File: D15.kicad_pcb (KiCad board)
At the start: 4 copper layers, 76 x 11 mm, 73 parts, among them IC1 DRV8847RTER, IC2 NCP730BM, J2 Conn_01x01, J3 Conn_01x01, J4 Conn_01x01, J5 UDPI, Q1 BC857BDW1, Q2 BC847BDW1, Q3 BC847BDW1, U1 AVR-64DA32, U3 BNO055, U4 TPS22810DRVR, m1 MountingHole_Pad

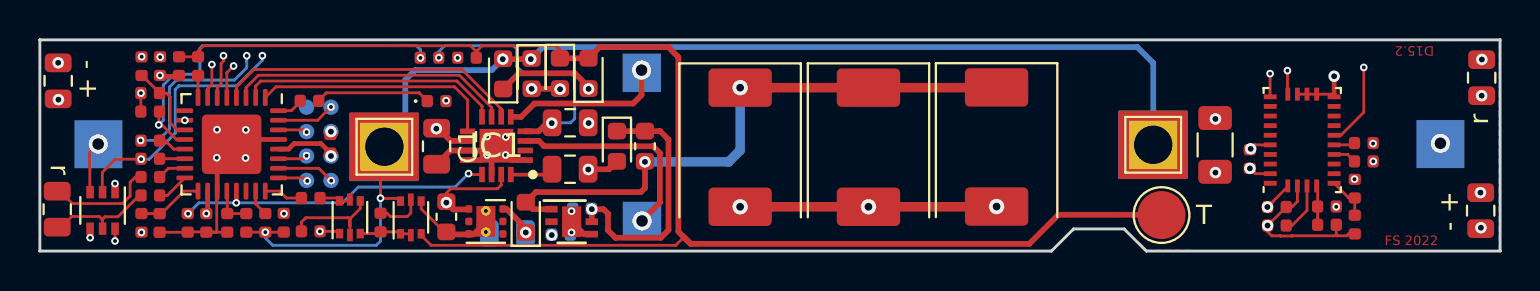
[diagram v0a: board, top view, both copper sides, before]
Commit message: Changed H-Bridge, added hardware PWM
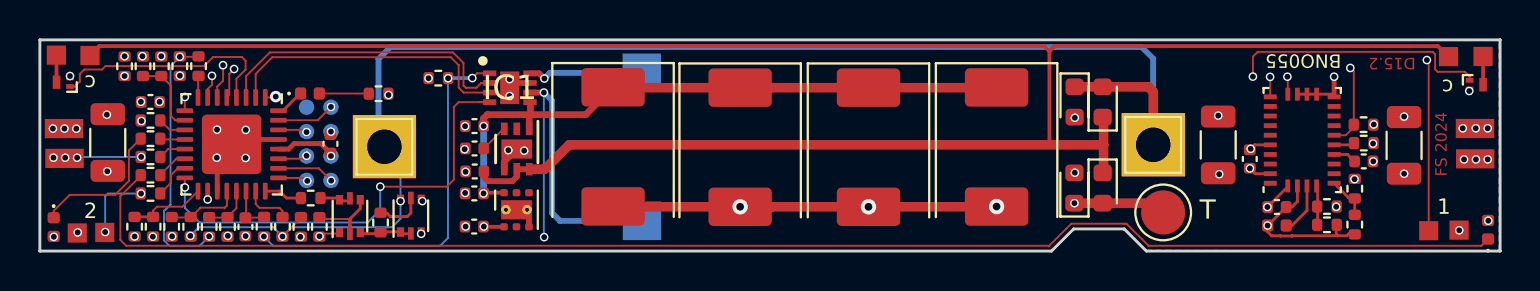
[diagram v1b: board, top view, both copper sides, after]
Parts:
- removed C16, C19, C20: Dummy, Capacitor_SMD:C_0805_2012Metric
- removed D9: CDBURT0530, Diode_SMD:D_0603_1608Metric
- removed H1, H3: MountingHole, TestPoint:TestPoint_THTPad_2.5x2.5mm_Drill1.2mm
- removed L1: 1uH, Inductor_SMD:L_0603_1608Metric
- added C3: 330u/25V, Capacitor_Tantalum_SMD:CP_EIA-7361-38_AVX-V, F.Cu at (80.1, -43.2)
- added C4: 220u/6V, Capacitor_SMD:C_1206_3216Metric, F.Cu at (111.6, -43.3)
- added D5: white, LED_SMD:LED_0402_1005Metric, F.Cu at (125.6, -38.9)
- added J1: Conn_01x01, RTB:DummyNet-Connector, F.Cu at (53.6, -38.7)
- added J10: Conn_01x01, RTB:DummyNet-Connector, F.Cu at (51.5, -44.1)
- added J11: Conn_01x01, RTB:DummyNet-Connector, F.Cu at (124.9, -44.1)
- added J12: Conn_01x01, RTB:DummyNet-Connector, F.Cu at (125.0, -42.5)
- added J13: Conn_01x01, RTB:DummyNet-Connector, F.Cu at (51.1, -48.0)
- added J14: Conn_01x01, RTB:DummyNet-Connector, F.Cu at (125.4, -47.9)
- added J15: Conn_01x01, RTB:DummyNet-Connector, F.Cu at (52.9, -47.9)
- added J16: Conn_01x01, RTB:DummyNet-Connector, F.Cu at (123.6, -47.9)
- added J6: Conn_01x01, RTB:DummyNet-Connector, F.Cu at (52.2, -38.7)
- added J7: Conn_01x01, RTB:DummyNet-Connector, F.Cu at (124.1, -38.8)
- added J8: Conn_01x01, RTB:DummyNet-Connector, F.Cu at (122.5, -38.8)
- added J9: Conn_01x01, RTB:DummyNet-Connector, F.Cu at (51.5, -42.6)
- added Q4: PMZB200UNEYL, Package_DFN_QFN:Diodes_DFN1006-3, F.Cu at (125.0, -46.4)
- added R27: 3.3k, Resistor_SMD:R_0402_1005Metric, F.Cu at (54.6, -47.4)
- C1: value 4.7u/25V -> 100n/50V; footprint Capacitor_SMD:C_0805_2012Metric -> Capacitor_SMD:C_0402_1005Metric
- C11: value 100u/16V -> 100n/50V; footprint Capacitor_SMD:C_0805_2012Metric -> Capacitor_SMD:C_0402_1005Metric; moved to F.Cu
- C12: value 47uF -> 4.7u/6V; footprint Capacitor_SMD:C_0603_1608Metric -> Capacitor_SMD:C_0402_1005Metric
- C14: value 220uF -> 220u/6V
- C15: value Dummy -> 220u/6V; footprint Capacitor_SMD:C_0805_2012Metric -> Capacitor_SMD:C_1206_3216Metric
- C17, C18, C7: value 100u/25V -> 330u/25V
- C2: value 2.2nF -> 100n; moved to F.Cu
- C5: value 100nF -> 100n/50V; moved to F.Cu
- D1: value CDBURT0530 -> white; footprint Diode_SMD:D_0603_1608Metric -> LED_SMD:LED_0402_1005Metric
- IC1: value DRV8847RTER -> DRV8231ADSGR; footprint _Samac:QFN50P300X300X80-17N-D -> RTB:SON50P200X200X80-9N
- J5: value UDPI -> UDPI & Debug IF
- Q3: value BC847BDW1 -> PMZB200UNEYL; footprint Package_TO_SOT_SMD:SOT-363_SC-70-6 -> Package_DFN_QFN:Diodes_DFN1006-3
- R10, R12: value 68k -> 47k
- R16: value 200 -> 3.3k; footprint Resistor_SMD:R_0805_2012Metric -> Resistor_SMD:R_0402_1005Metric
- R17: value 10k -> 3.3k
- R2: value 0.3 -> 33k; footprint Resistor_SMD:R_0805_2012Metric -> Resistor_SMD:R_0402_1005Metric
- R26, R4, R6: value 2.2k -> 3.3k
- moved C15 71.6 mm to (53.8, -43.4)
- moved R2 41.3 mm to (119.1, -44.3), turned to 180 degrees
- moved D7 31.2 mm to (105.6, -45.5)
- moved D8 28.3 mm to (104.1, -45.5)
- moved D2 27.4 mm to (104.1, -41.0), turned to 90 degrees
- moved D4 27.4 mm to (105.6, -41.0), turned to 270 degrees
- moved D1 24.6 mm to (51.0, -39.0), turned to 270 degrees
- moved R16 21.9 mm to (56.0, -40.8), turned to 180 degrees
- moved R17 15.1 mm to (71.0, -46.8), turned to 0 degrees
- moved R19 15.0 mm to (57.5, -47.4), turned to 90 degrees
- moved R9 12.3 mm to (61.9, -39.0), turned to 90 degrees
- moved C14 9.84 mm to (121.2, -43.2)
- moved R36 9.08 mm to (60.0, -39.0), turned to 270 degrees
- moved R34 8.51 mm to (59.1, -39.0), turned to 90 degrees
- moved C22 7.78 mm to (60.9, -39.0), turned to 270 degrees
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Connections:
- C11 pad 1: Net-(C11-Pad1) -> VHBR
- C15 pad 1: Net-(C15-Pad1) -> +3V3
- C15 pad 2: Net-(C15-Pad2) -> GND
- C5 pad 1: Net-(C5-Pad1) -> VTRK
- D1 pad 1: Net-(C11-Pad1) -> Net-(D1-Pad1)
- D1 pad 2: VHBR -> +3V3
- D3 pad 1: Net-(D3-Pad1) -> LED.hbt
- D3 pad 2: +3V3 -> Net-(D3-Pad2)
- IC1 pad 1: GND -> Net-(IC1-Pad1)
- IC1 pad 2: (no net) -> PWM1
- IC1 pad 3: M2 -> PWM2
- IC1 pad 4: Net-(IC1-Pad4) -> Vref
- IC1 pad 5: M1 -> VHBR
- IC1 pad 6: ~FAULT -> M2
- IC1 pad 7: PWM1 -> GND
- IC1 pad 8: PWM2 -> M1
- IC1 pad 9: TRQ -> GND
- IC2 pad 6: Net-(C11-Pad1) -> VHBR
- Q3 pad 1: GND -> COUPLER.1
- Q3 pad 2: Net-(C15-Pad1) -> GND
- Q3 pad 3: LAMP.F -> Net-(J13-Pad1)
- R1 pad 2: Net-(C16-Pad1) -> Net-(J9-Pad1)
- R16 pad 1: Net-(IC1-Pad16) -> LED.aux2
- R16 pad 2: VTRK -> Net-(J1-Pad1)
- R17 pad 1: ACK -> GND
- R17 pad 2: GND -> Net-(IC1-Pad1)
- R2 pad 1: Net-(IC1-Pad4) -> GND
- R2 pad 2: GND -> BNO.res
- R26 pad 1: LED.hbt -> Net-(D3-Pad2)
- R26 pad 2: Net-(D3-Pad1) -> +3V3
- R4 pad 2: Net-(C15-Pad1) -> Net-(J11-Pad1)
- R5 pad 1: LED.F.red -> LED.F.cab
- R5 pad 2: Net-(C16-Pad2) -> Net-(D1-Pad1)
- R6 pad 1: LED.R.red -> LED.R.cab
- R6 pad 2: Net-(C15-Pad2) -> Net-(D5-Pad1)
- R9 pad 1: Net-(IC1-Pad4) -> Net-(IC1-Pad1)
- U1 pad 1: TRQ -> COUPLER.2
- U1 pad 10: UDCC-a -> uSENS1
- U1 pad 11: uSENS1 -> LED.R.wht
- U1 pad 12: ISENS -> LED.F.cab
- U1 pad 13: LED.R.red -> LED.F.wht
- U1 pad 14: LED.R.wht -> LED.R.cab
- U1 pad 15: LED.F.red -> LED.aux2
- U1 pad 16: LED.F.wht -> Vref
- U1 pad 21: ACK -> UDCC-a
- U1 pad 22: (no net) -> ISENS
- U1 pad 4: ~FAULT -> COUPLER.1
- U1 pad 9: (no net) -> LED.aux1
- U4 pad 5: Net-(C5-Pad1) -> VTRK
- U4 pad 6: Net-(C5-Pad1) -> VTRK
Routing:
- net VTRK: track 11.5 -> 112.9 mm, vias 2 -> 0
- net LAMP.R: track 81.8 -> 0.00 mm, vias 2 -> 0
- net Net-(J11-Pad1): track 0.00 -> 81.2 mm, vias 0 -> 4
- net Net-(C15-Pad1): track 78.7 -> 0.00 mm, vias 3 -> 0
- net Net-(J8-Pad1): track 0.00 -> 77.4 mm, vias 0 -> 2
- net Net-(C15-Pad2): track 76.6 -> 0.00 mm, vias 3 -> 0
- net Net-(D5-Pad1): track 0.00 -> 76.2 mm
- net COUPLER.2: track 0.00 -> 66.4 mm, vias 0 -> 2
- net Vref: track 0.00 -> 23.8 mm, vias 0 -> 2
- net Net-(IC1-Pad1): track 0.00 -> 20.5 mm, vias 0 -> 3
- net ISENS: track 19.8 -> 2.38 mm, vias 2 -> 0
- net ACK: track 16.9 -> 0.00 mm, vias 3 -> 0
- net GND: track 49.2 -> 33.1 mm, vias 32 -> 43
- net ~FAULT: track 16.0 -> 0.00 mm
- net Net-(IC1-Pad4): track 14.2 -> 0.00 mm, vias 2 -> 0
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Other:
- net class Default: trace_width 0.15 -> 0.1; via_dia 0.6 -> 0.45
- rule pad_to_mask_clearance: 0.2 -> 0
- rule trace_min: 0.15 -> 0.1
- rule via_min_drill: 0.2 -> 0.3
- rule via_min_size: 0.4 -> 0.45
- board text added: "1"
- board text added: "2"
- board text added: "BNO055"
- board text added: "FS 2024"
- board text added: "M1"
- board text added: "M2"
- board text added: "c"
- board text removed: "- +"
- board text removed: "FS 2022"
- board text removed: "r"

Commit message: add: decoder lock
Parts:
- removed J5: UDPI & Debug IF, Connector_PinHeader_1.27mm:PinHeader_2x04_P1.27mm_Vertical
- added J17: Conn_01x01, RTB:DummyNet-Connector, F.Cu at (64.4, -41.8)
- moved C6 1.13 mm to (64.3, -43.1), turned to 180 degrees
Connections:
- U1 pad 25: V24.rts -> (no net)
- U1 pad 26: V24.cts -> (no net)
- U1 pad 30: V24.tx -> (no net)
- U1 pad 31: V24.rx -> (no net)
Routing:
- net V24.rx: track 3.03 -> 0.00 mm, vias 1 -> 0
- net V24.cts: track 3.01 -> 0.00 mm, vias 1 -> 0
- net +3V3: track 17.9 -> 16.0 mm
- net V24.rts: track 1.56 -> 0.00 mm, vias 1 -> 0
- net V24.tx: track 1.51 -> 0.00 mm, vias 1 -> 0
- net UPDI: track 1.52 -> 2.03 mm, vias 1 -> 0
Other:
- board text added: "D15.3"
- board text added: "U"
- board text removed: "D15.2"

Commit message: mod: led automation
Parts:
- C10, C13, C6: value 1u -> 100n
- D4, D7, D8: value D -> CDBURT0530
- R10, R12: value 47k -> 33k
- R11, R13: value 10k -> 12k
- R17: value 3.3k -> 1k
- renumbered m1 to H1
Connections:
- net COUPLER.1 renamed AUX.5
- net COUPLER.2 renamed AUX.6
- net LED.aux1 renamed AUX.3
- net LED.aux2 renamed AUX.4
